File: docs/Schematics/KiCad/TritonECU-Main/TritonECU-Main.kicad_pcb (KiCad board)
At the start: 4 copper layers, 158 x 174 mm, 450 parts, among them J1 EEC-V 104, J1001 TACH/SPEED, J301 VR spare, J901 USB4105-GF-A, J902 104031-0811, Q101 ISL9V3040S3ST, Q102 ISL9V3040S3ST, Q103 ISL9V3040S3ST, Q104 ISL9V3040S3ST, Q105 ISL9V3040S3ST, Q106 ISL9V3040S3ST, Q107 ISL9V3040S3ST, Q108 ISL9V3040S3ST, Q109 BSS138, Q201 ZXMS6005DGQTA, Q202 ZXMS6005DGQTA, Q203 ZXMS6005DGQTA, Q204 ZXMS6005DGQTA, Q205 ZXMS6005DGQTA, Q206 ZXMS6005DGQTA, Q207 ZXMS6005DGQTA, Q208 ZXMS6005DGQTA, Q401 NCV8405ASTT1G, Q402 NCV8405ASTT1G, Q403 NCV8405ASTT1G, Q404 NCV8405ASTT1G, Q405 NCV8405ASTT1G, Q406 NCV8405ASTT1G, Q407 NCV8405ASTT1G, Q408 NCV8405ASTT1G, Q501 NCV8405ASTT1G, Q502 NCV8405ASTT1G, Q503 NCV8405ASTT1G, Q504 NCV8408BDTRKG, Q505 NCV8405ASTT1G, Q506 NCV8405ASTT1G, Q507 NCV8405ASTT1G, Q701 DMN6040SVTQ-7, Q702 DMN6040SVTQ-7, U001 TPS22917DBVR, U002 TPS22917DBVR, U101 74HCT541, U102 TPS3823A-33DBVR, U301 MAX9926UAEE+T, U302 MAX9926UAEE+T, U303 MAX9926UAEE+T, U401 74HCT541, U402 74HC4051, U501 74HCT541, U601 TBD62083AFNG, U701 NCV8772CDT504RKG, U702 TPS2H160BQPWPRQ1, U703 LM74700QDBVRQ1, U704 LM74700QDBVRQ1, U801 ADS8588HIPM, U802 MAX6070AAUT25+T, U803 OPA2376AQDRQ1, U804 OPA2376AQDRQ1, U805 TLV9064QPWRQ1, U806 MAX6070AAUT18+T, U901 DRV8837DSGR, U902 TLV7031DBVR, U903 TJA1042T/3, U904 USBLC6-2SC6, U905 TPS22917DBVR

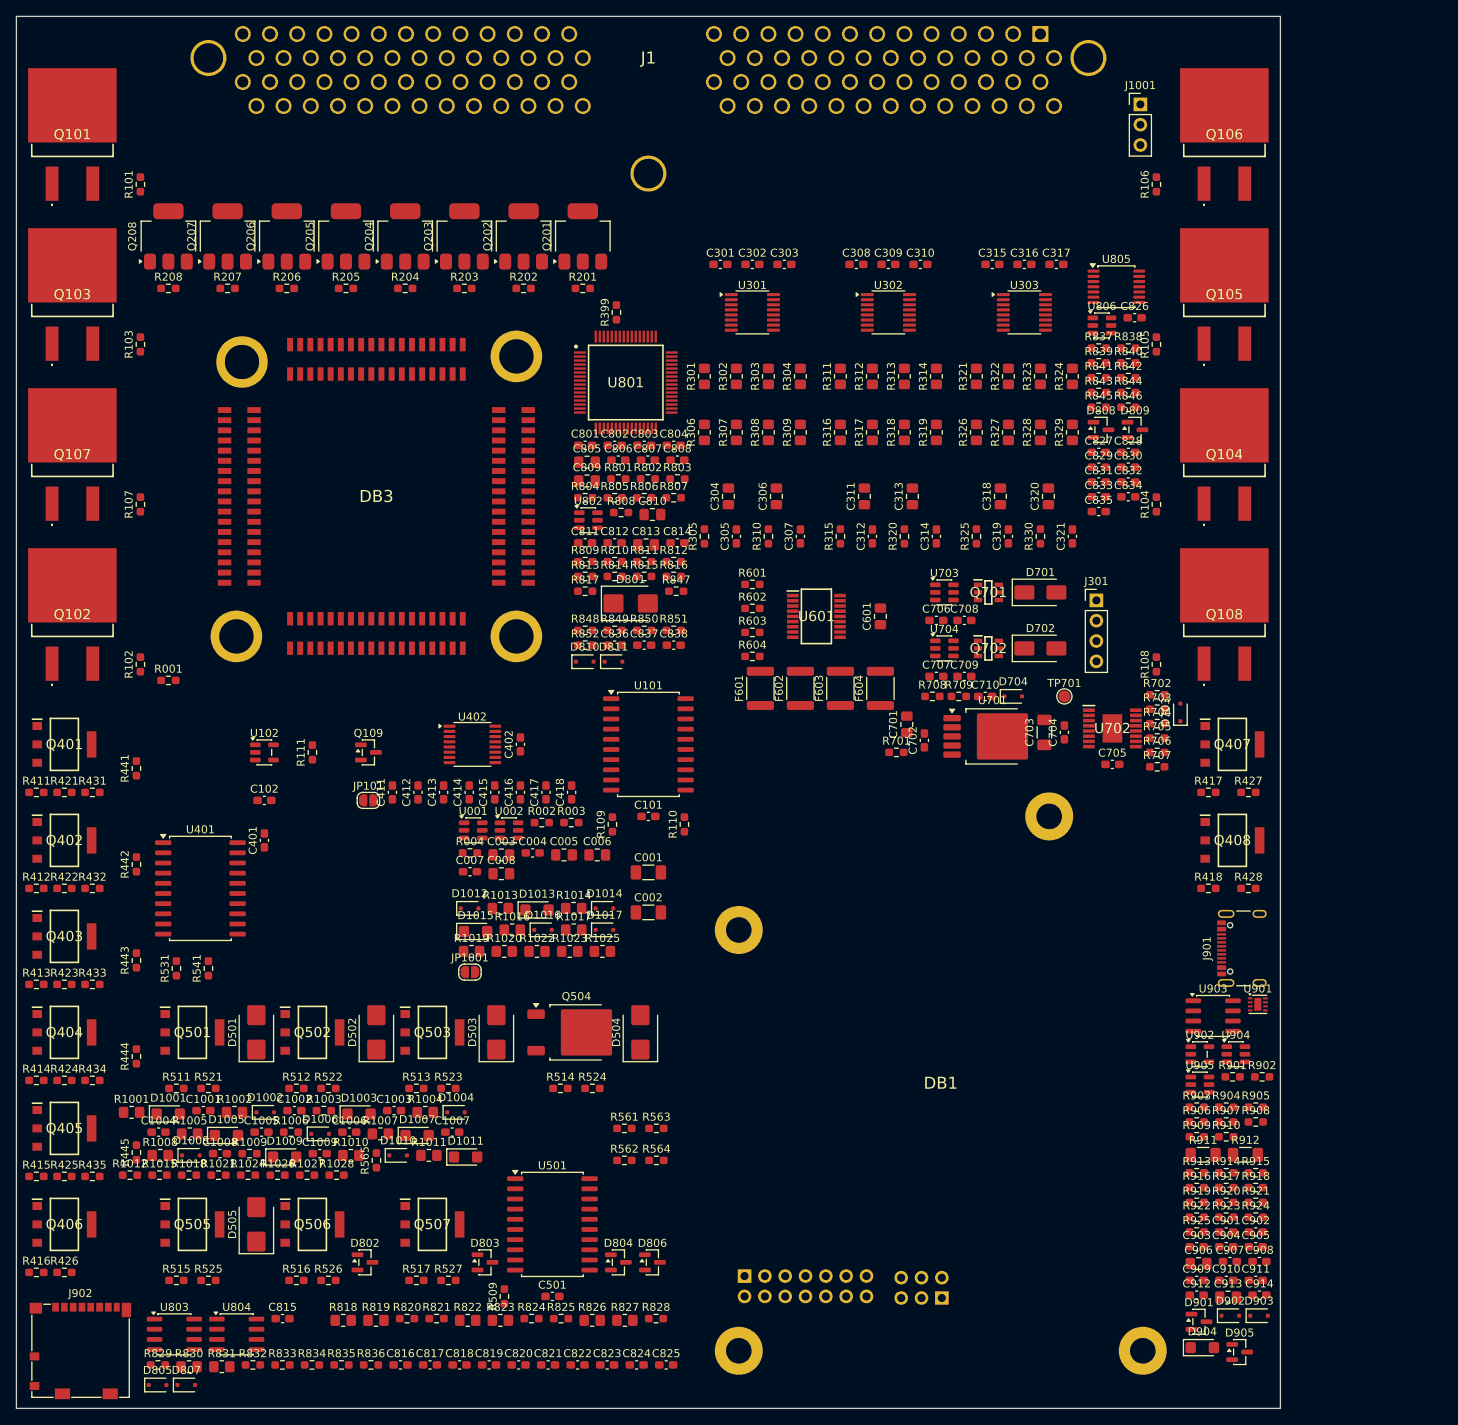
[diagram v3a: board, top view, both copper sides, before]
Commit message: Carrier: AGND star, matched ADC returns, 6-layer route
- ADC core, reference and inputs move to a separate AGND net, joined to
  GND and SIGRTN only at NT801 (the star under EEC-V 91). TPS/CHT/IAT/VREF
  VxGND inputs return on SIGRTN.
- Matched 0R legs on AIN_nGND (R853-R856), R857 bleed and D812 clamp on
  MAF_G, per ADS8588H SBAS843A.
- PCB generator syncs schematic fields onto existing footprints and packs
  the ADC column so the AGND island stays clear of GND parts.
- Board goes to 6 layers (1.6 mm): F / In1 GND plane with AGND island /
  In2-In4 signal / B. route_carrier.py adds net classes, the plane,
  Freerouting DSN/SES export/import and a repair mode that pre-stitches
  GND/AGND pads to the plane. Freerouting plus hand routing: DRC 0
  errors, 0 unconnected, schematic parity clean (silkscreen still to tidy).

Co-Authored-By: Claude Opus 5.5 <noreply@anthropic.com>
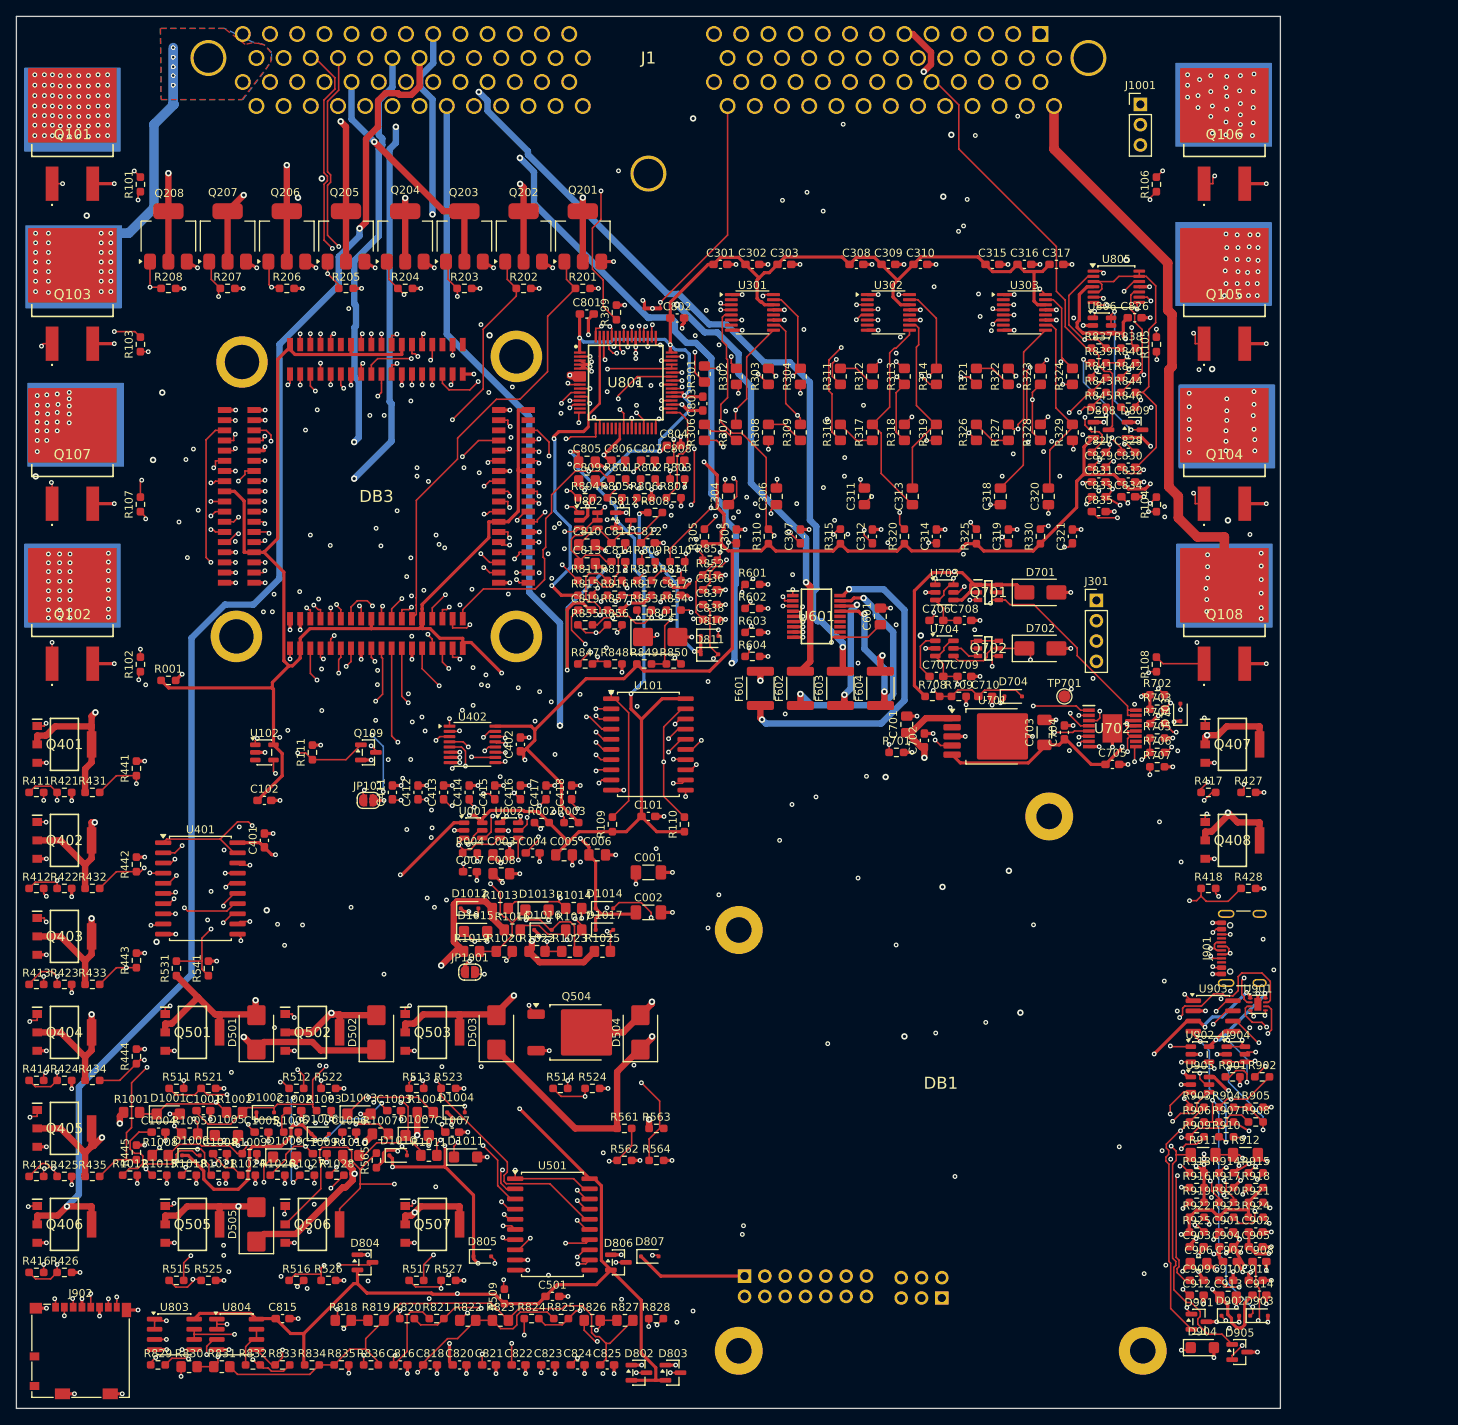
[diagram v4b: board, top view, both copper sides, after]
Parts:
- added D812: BAV199, Package_TO_SOT_SMD:SOT-23, F.Cu at (100.9, 88.0)
- added NT801: NetTie_3, NetTie:NetTie-3_SMD_Pad0.5mm, F.Cu at (104.5, 61.5)
- added R853: 0, Resistor_SMD:R_0603_1608Metric_Pad0.98x0.95mm_HandSolder, F.Cu at (103.5, 99.2)
- added R854: 0, Resistor_SMD:R_0603_1608Metric_Pad0.98x0.95mm_HandSolder, F.Cu at (107.2, 99.2)
- added R855: 0, Resistor_SMD:R_0603_1608Metric_Pad0.98x0.95mm_HandSolder, F.Cu at (96.1, 101.1)
- added R856: 0, Resistor_SMD:R_0603_1608Metric_Pad0.98x0.95mm_HandSolder, F.Cu at (99.8, 101.1)
- added R857: 10k, Resistor_SMD:R_0603_1608Metric_Pad0.98x0.95mm_HandSolder, F.Cu at (99.8, 99.2)
- moved C817 100.9 mm to (107.2, 97.4)
- moved C819 95.1 mm to (96.1, 99.2)
- moved D807 60.1 mm to (104.2, 180.0)
- moved D805 43.7 mm to (83.2, 180.0)
- moved D802 36.9 mm to (102.8, 194.5)
- moved D804 31.7 mm to (68.6, 180.7)
- moved D803 27.2 mm to (107.1, 194.5)
- moved R852 17.9 mm to (111.7, 94.8)
- moved C802 17.7 mm to (107.6, 62.7)
- moved C801 16.4 mm to (96.3, 62.2)
- moved D810 15.9 mm to (111.6, 102.4)
- moved R847 14.6 mm to (96.1, 105.9)
- moved C836 13.8 mm to (111.7, 96.7)
- moved D811 12.0 mm to (111.6, 104.7)
- moved R851 9.87 mm to (111.7, 93.0)
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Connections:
- C801 pad 2: GND -> AGND
- C802 pad 2: GND -> AGND
- C803 pad 2: GND -> AGND
- C804 pad 2: GND -> AGND
- C805 pad 2: GND -> AGND
- C806 pad 2: GND -> AGND
- C807 pad 2: GND -> AGND
- C808 pad 2: GND -> AGND
- C809 pad 2: GND -> AGND
- C810 pad 2: GND -> AGND
- C811 pad 2: GND -> AGND
- C812 pad 2: GND -> AGND
- C813 pad 2: GND -> AGND
- C814 pad 2: GND -> AGND
- C817 pad 2: GND -> AGND
- C819 pad 2: GND -> AGND
- R802 pad 2: GND -> AGND
- R803 pad 2: GND -> AGND
- R804 pad 2: GND -> AGND
- R805 pad 2: GND -> AGND
- R806 pad 2: GND -> AGND
- R807 pad 2: GND -> AGND
- R809 pad 2: GND -> AGND
- R817 pad 2: GND -> AGND
- U801 pad 2: GND -> AGND
- U801 pad 26: GND -> AGND
- U801 pad 3: GND -> AGND
- U801 pad 34: GND -> AGND
- U801 pad 35: GND -> AGND
- U801 pad 4: GND -> AGND
- U801 pad 40: GND -> AGND
- U801 pad 41: GND -> AGND
- U801 pad 43: GND -> AGND
- U801 pad 46: GND -> AGND
- U801 pad 47: GND -> AGND
- U801 pad 5: GND -> AGND
- U801 pad 50: MAF_RTN -> /ADC/MAF_G
- U801 pad 52: GND -> /ADC/TPS_G
- U801 pad 54: GND -> AGND
- U801 pad 56: GND -> AGND
- U801 pad 58: GND -> /ADC/CHT_G
- U801 pad 60: GND -> /ADC/IAT_G
- U801 pad 62: GND -> AGND
- U801 pad 64: GND -> SIGRTN
- U802 pad 2: GND -> AGND
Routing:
- net +3.3V: track 0.00 -> 647.1 mm, vias 0 -> 23
- net +5V_SW: track 0.00 -> 415.1 mm, vias 0 -> 12
- net GND: track 0.00 -> 361.1 mm, vias 0 -> 277
- net SD_D0: track 0.00 -> 287.1 mm, vias 0 -> 4
- net SD_CMD: track 0.00 -> 283.2 mm, vias 0 -> 7
- net +3.3V_SW: track 0.00 -> 275.2 mm, vias 0 -> 11
- net +5V: track 0.00 -> 257.2 mm, vias 0 -> 11
- net CAN_L: track 0.00 -> 254.9 mm, vias 0 -> 5
- net VPWR: track 0.00 -> 250.5 mm, vias 0 -> 7
- net CAN_H: track 0.00 -> 245.0 mm, vias 0 -> 4
- net /Inputs/TACH_H: track 0.00 -> 241.0 mm, vias 0 -> 2
- net VENT_OUT: track 0.00 -> 239.6 mm, vias 0 -> 3
- net IAC_OUT: track 0.00 -> 238.7 mm, vias 0 -> 4
- net SCP_P: track 0.00 -> 237.2 mm, vias 0 -> 3
- net O2_22_IN: track 0.00 -> 235.4 mm, vias 0 -> 2
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- added copper zone on In1.Cu, net AGND
- added copper zone on B.Cu, net COIL3_OUT
- added copper zone on F.Cu, net COIL3_OUT
- added copper zone on In1.Cu, net GND
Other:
- copper layers 4 -> 6
